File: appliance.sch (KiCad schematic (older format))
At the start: 32 parts, among them J2 Jlink-Tag connect, Q1 pmos, U2 AP2112K-3.3, U3 MCP73831-2-OT

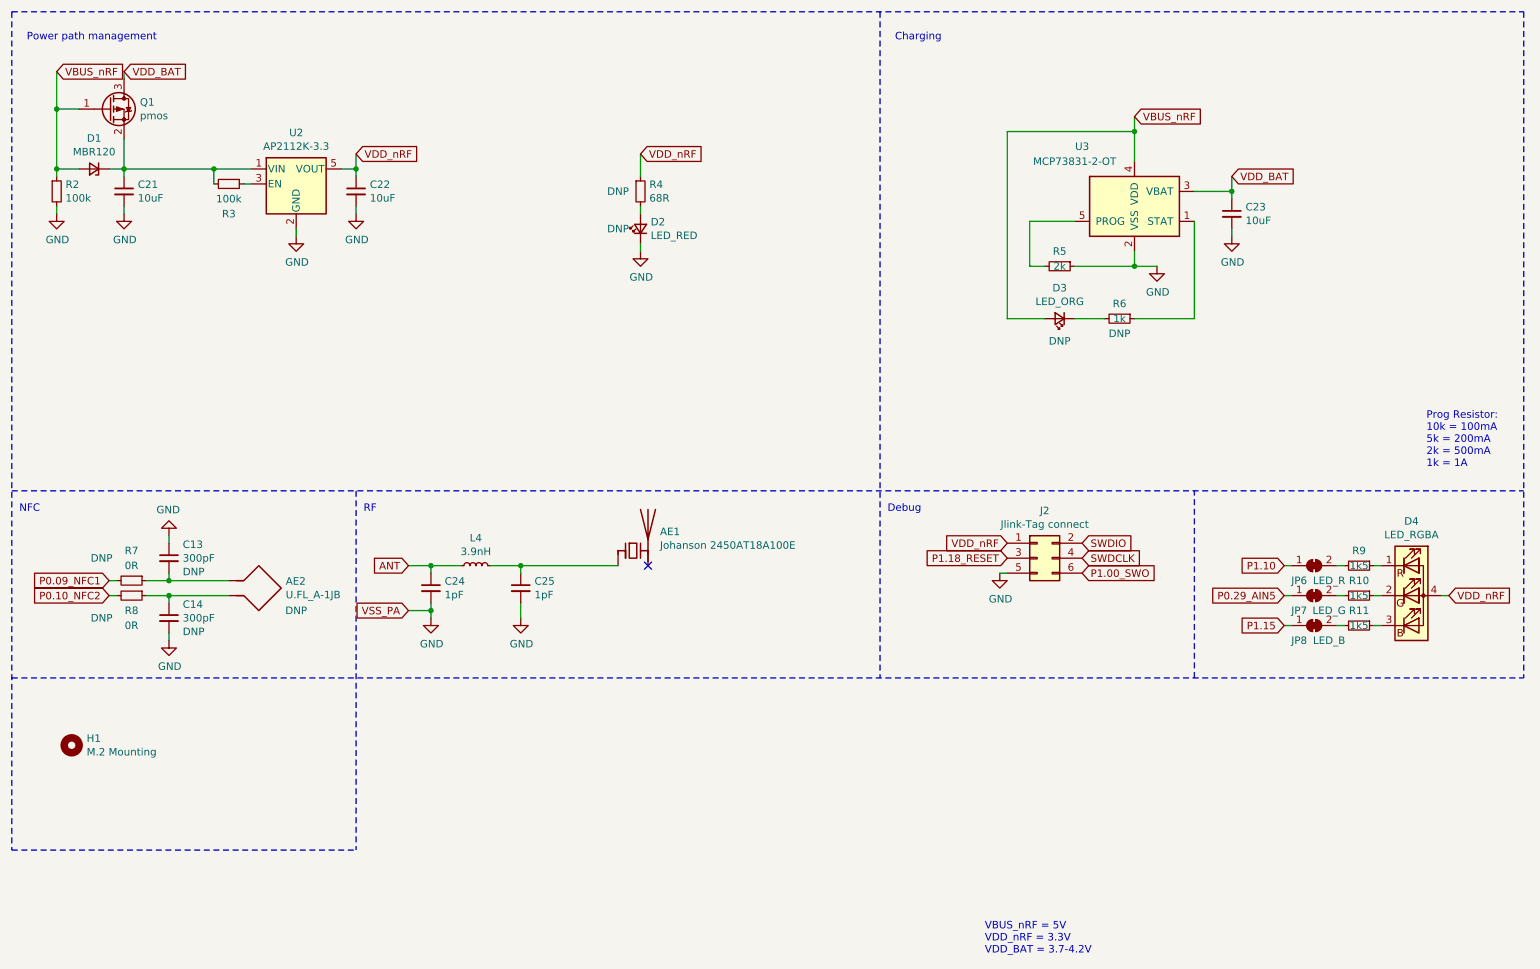
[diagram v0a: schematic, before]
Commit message: update 3D/docs/fiducials
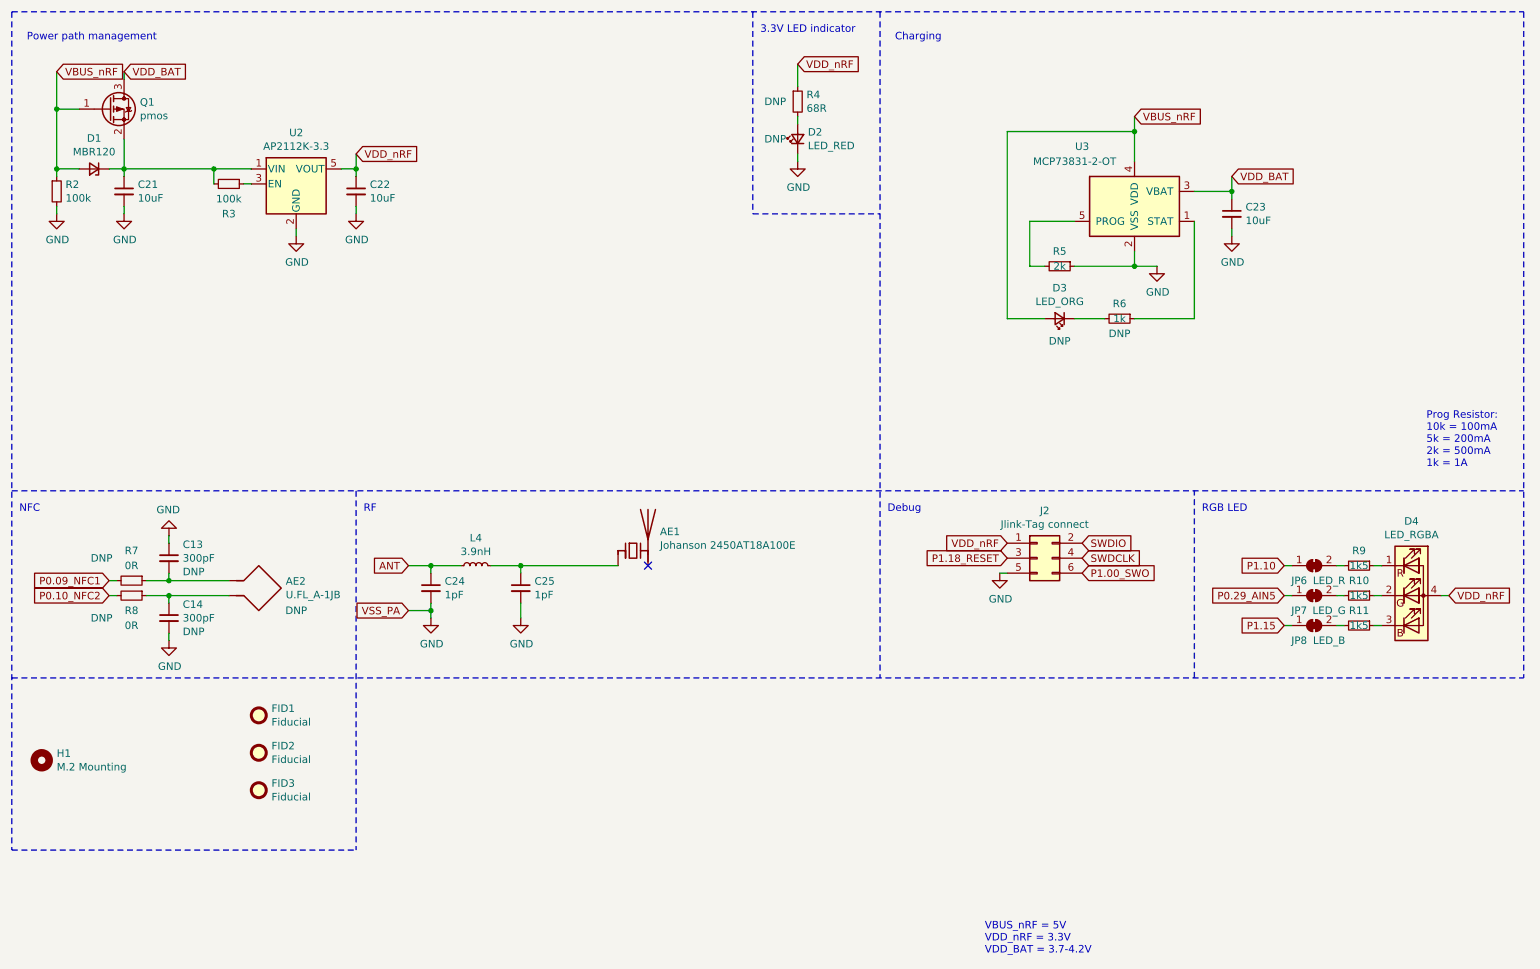
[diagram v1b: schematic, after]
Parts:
- added FID1, FID2, FID3: Fiducial, Fiducial:Fiducial_0.5mm_Mask1mm, symbol Mechanical:Fiducial
- AE1: Description (none) -> RF ANT 2.4GHZ CHIP SOLDER SMD; Digikey (none) -> 712-1005-1-ND; LCSC (none) -> C89334; MFG P/N (none) -> 2450AT18A100E; Manufacturer (none) -> Johanson Technology Inc.
- AE2: Description (none) -> CONN UMC JACK STR 50 OHM SMD; Digikey (none) -> ARF1579CT-ND; LCSC (none) -> C88373; MFG P/N (none) -> A-1JB; Manufacturer (none) -> Amphenol RF Division
- C24, C25: Description (none) -> CAP CER 1PF 50V C0G/NPO 0402; Digikey (none) -> 311-2076-1-ND; LCSC (none) -> C277493; MFG P/N (none) -> CC0402CRNPO9BN1R0; Manufacturer (none) -> Yageo
- D4: Description (none) -> LED RGB DIFFUSED CHIP SMD; Digikey (none) -> 160-2162-1-ND; LCSC (none) -> C458749; MFG P/N (none) -> LTST-C19HE1WT; Manufacturer (none) -> Lite-On Inc.
- H1, J2, JP6, JP7, JP8: DNP (none) -> DNP
- L4: Description (none) -> FIXED IND 3.9NH 700MA 190 MOHM; Digikey (none) -> 490-1079-1-ND; LCSC (none) -> C97987; MFG P/N (none) -> LQG15HN3N9S02D; Manufacturer (none) -> Murata Electronics
- R10, R11, R9: Description (none) -> RES SMD 1.5K OHM 1% 1/16W 0402; Digikey (none) -> 311-1.50KLRCT-ND; LCSC (none) -> C114759; MFG P/N (none) -> RC0402FR-071K5L; Manufacturer (none) -> Yageo
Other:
- note added: "3.3V LED indicator"
- note added: "RGB LED"
- moved on the sheet: D2, H1, R4

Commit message: adjust m.2 mounting diameter
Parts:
- H1: footprint MountingHole:MountingHole_2.2mm_M2_Pad -> MountingHole:MountingHole_3.2mm_M3
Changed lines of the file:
@@
 Sheet 3 3
 Title "nrf52840_m.2 module"
-Date "2020-12-02"
-Rev "0.1"
-Comp "crohloff Engineering"
+Date "2021-05-13"
+Rev "1.0"
+Comp ""
 Comment1 ""
 Comment2 ""
@@
 F 0 "H1" H 800 5546 50  0000 L CNN
 F 1 "M.2 Mounting" H 800 5455 50  0000 L CNN
-F 2 "MountingHole:MountingHole_2.2mm_M2_Pad" H 700 5500 50  0001 C CNN
+F 2 "MountingHole:MountingHole_3.2mm_M3" H 700 5500 50  0001 C CNN
 F 3 "" H 700 5500 50  0001 C CNN
 F 4 "DNP" H 700 5500 50  0001 C CNN "DNP"
